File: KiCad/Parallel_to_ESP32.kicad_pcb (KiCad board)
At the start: 2 copper layers, 47 x 50 mm, 21 parts, among them J1 DB25_Male, J2 Micro_SD_Card_Socket, J3 Conn_01x02, J4 Conn_01x02, U1 ESP32-DEVKIT-V1, U2 SN74CB3T16210

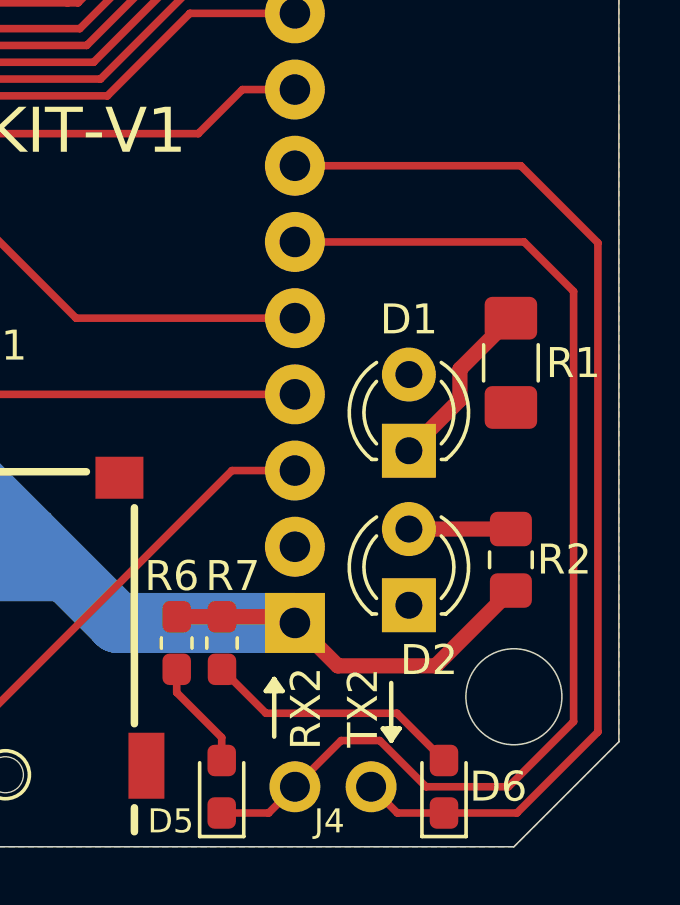
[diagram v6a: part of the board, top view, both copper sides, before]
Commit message: fixed activity LED circuit using a PNP-transistor
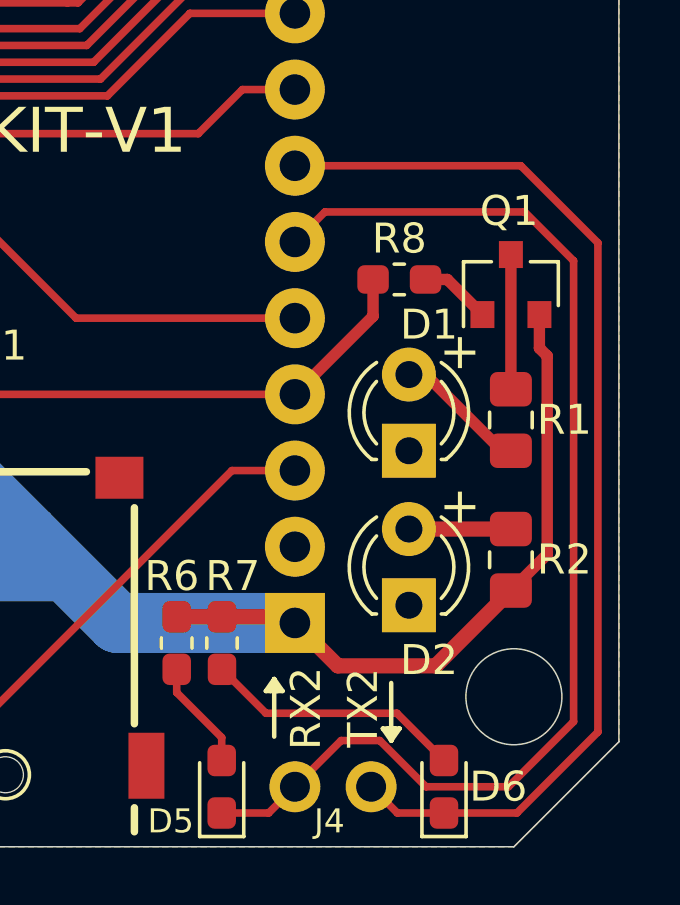
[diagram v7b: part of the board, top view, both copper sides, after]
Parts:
- added Q1: 2N3906, Package_TO_SOT_SMD:SOT-23, F.Cu at (167.6, 116.3)
- added R8: 1k, Resistor_SMD:R_0603_1608Metric_Pad1.05x0.95mm_HandSolder, F.Cu at (163.9, 116.1)
- R1: footprint Resistor_SMD:R_1206_3216Metric_Pad1.42x1.75mm_HandSolder -> Resistor_SMD:R_0805_2012Metric_Pad1.15x1.40mm_HandSolder
- moved R1 1.91 mm to (167.6, 120.8)
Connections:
- D1 pad 1: Net-(D1-Pad1) -> GND
- D1 pad 2: ACT_LED -> Net-(D1-Pad2)
- R1 pad 1: Net-(D1-Pad1) -> Net-(Q1-Pad3)
- R1 pad 2: GND -> Net-(D1-Pad2)
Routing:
- net 3V3: track 140.2 -> 150.0 mm
- net Net-(D1-Pad1): track 5.83 -> 0.00 mm
- net CS: track 13.6 -> 18.5 mm
- net Net-(Q1-Pad3): track 0.00 -> 4.49 mm
- net Net-(D1-Pad2): track 0.00 -> 4.45 mm
- net Net-(Q1-Pad1): track 0.00 -> 2.38 mm
- net RX2: track 38.6 -> 40.0 mm
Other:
- board text added: "+"

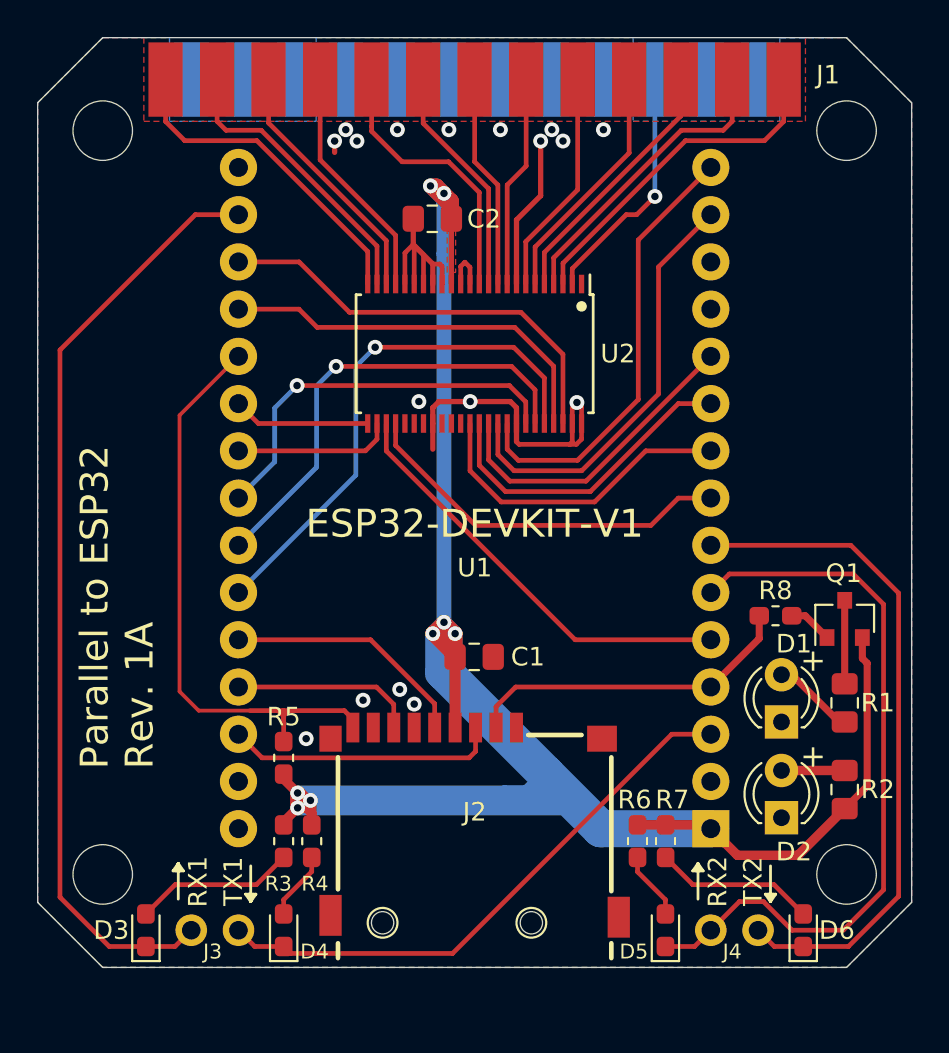
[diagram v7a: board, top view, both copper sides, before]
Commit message: Re-assignment of some pins and simplified Activity LED circuit
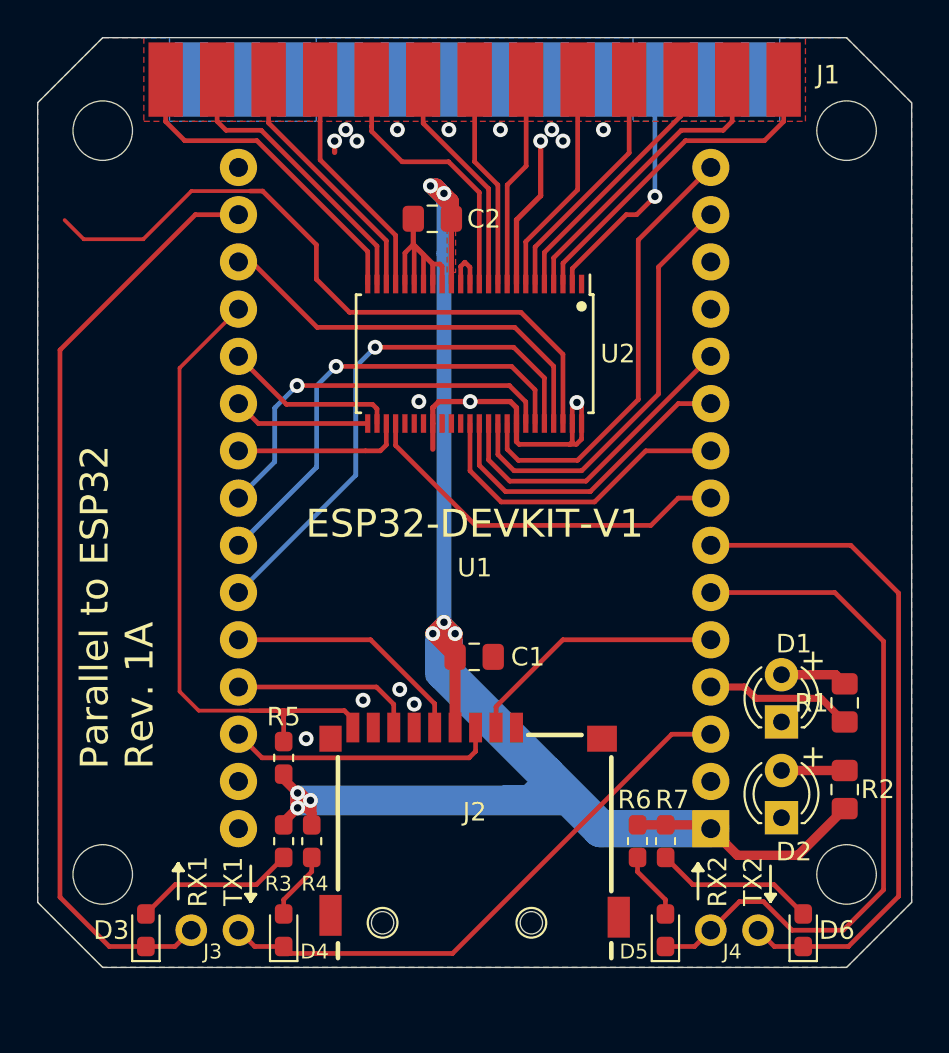
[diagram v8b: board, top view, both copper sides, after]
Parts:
- removed Q1: 2N3906, Package_TO_SOT_SMD:SOT-23
- removed R8: 1k, Resistor_SMD:R_0603_1608Metric_Pad1.05x0.95mm_HandSolder
- R1, R2: value 150 -> 200
- turned R1 to 90 degrees
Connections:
- net RX0 renamed Net-(U1-Pad12)
- net TX0 renamed Net-(U1-Pad13)
- J2 pad 9: CD -> CP
- R1 pad 1: Net-(Q1-Pad3) -> ACT_LED
- R5 pad 2: CD -> CP
- U1 pad 18: RESET_3V3 -> STROBE_3V3
- U1 pad 19: STROBE_3V3 -> CP
- U1 pad 20: CD -> POUT_3V3
- U1 pad 22: POUT_3V3 -> BUSY_3V3
- U1 pad 4: CS -> ACT_LED
- U1 pad 5: BUSY_3V3 -> CS
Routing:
- net CP: track 0.00 -> 35.0 mm
- net CD: track 32.4 -> 0.00 mm
- net BUSY_3V3: track 23.1 -> 9.23 mm
- net RESET_3V3: track 23.2 -> 36.7 mm
- net 3V3: track 150.0 -> 140.2 mm
- net ACT_LED: track 0.00 -> 7.98 mm
- net Net-(Q1-Pad3): track 4.49 -> 0.00 mm
- net CS: track 18.5 -> 14.7 mm
- net Net-(Q1-Pad1): track 2.38 -> 0.00 mm
- net RX2: track 40.0 -> 38.0 mm
- net STROBE_3V3: track 21.3 -> 22.4 mm
- net POUT_3V3: track 8.56 -> 9.41 mm
- net Net-(D1-Pad2): track 4.45 -> 3.60 mm
